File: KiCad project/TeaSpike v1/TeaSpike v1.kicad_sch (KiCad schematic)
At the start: 23 parts, among them U1 TP4056, U2 PowerBoost

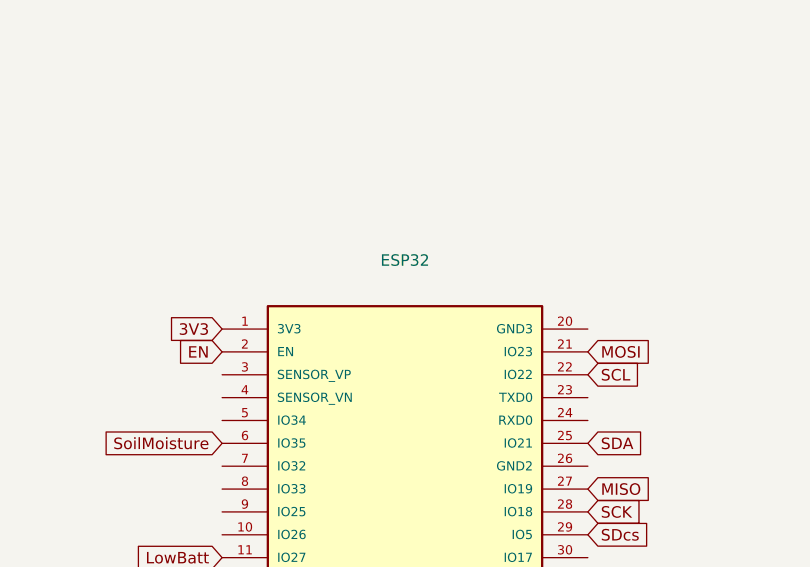
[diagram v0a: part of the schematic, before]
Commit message: Corregida huella PowerBoost
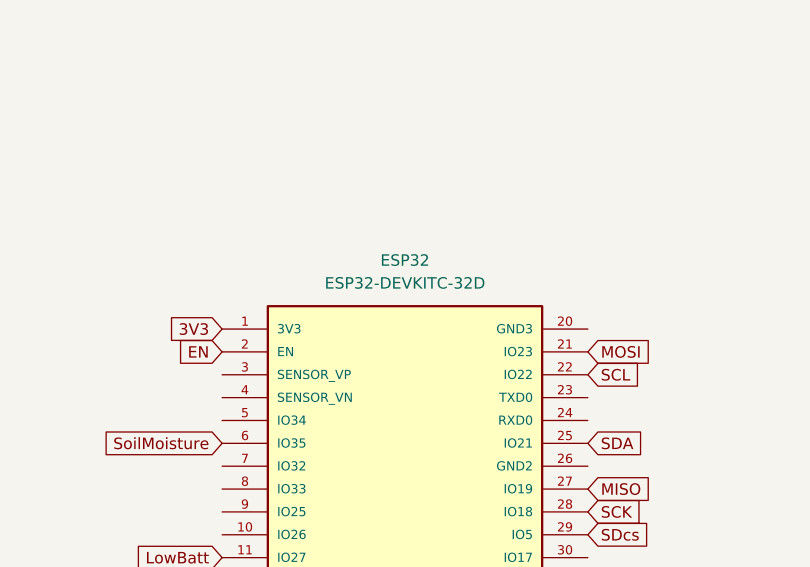
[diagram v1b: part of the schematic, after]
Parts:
- ESP32: value (none) -> ESP32-DEVKITC-32D; footprint (none) -> ESP32-DEVKITC-32D:MODULE_ESP32-DEVKITC-32D
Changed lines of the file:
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@@
     (in_bom yes) (on_board yes) (fields_autoplaced)
     (property "Reference" "ESP32" (id 0) (at 66.04 24.13 0))
-    (property "Value" "" (id 1) (at 66.04 26.67 0))
-    (property "Footprint" "" (id 2) (at 66.04 54.61 0)
+    (property "Value" "ESP32-DEVKITC-32D" (id 1) (at 66.04 26.67 0))
+    (property "Footprint" "ESP32-DEVKITC-32D:MODULE_ESP32-DEVKITC-32D" (id 2) (at 66.04 54.61 0)
       (effects (font (size 1.27 1.27)) (justify left bottom) hide)
     )
